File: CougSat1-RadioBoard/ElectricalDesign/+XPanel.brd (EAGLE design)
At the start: 79 x 90 mm, 66 parts, among them J1 ADCS Connector, J2 Low Gain +, J3 Low Gain -, J4 Low Gain Coax, J5 GPS Coax, J6 EPS Connector, U1 AD8515, U3 AD7291

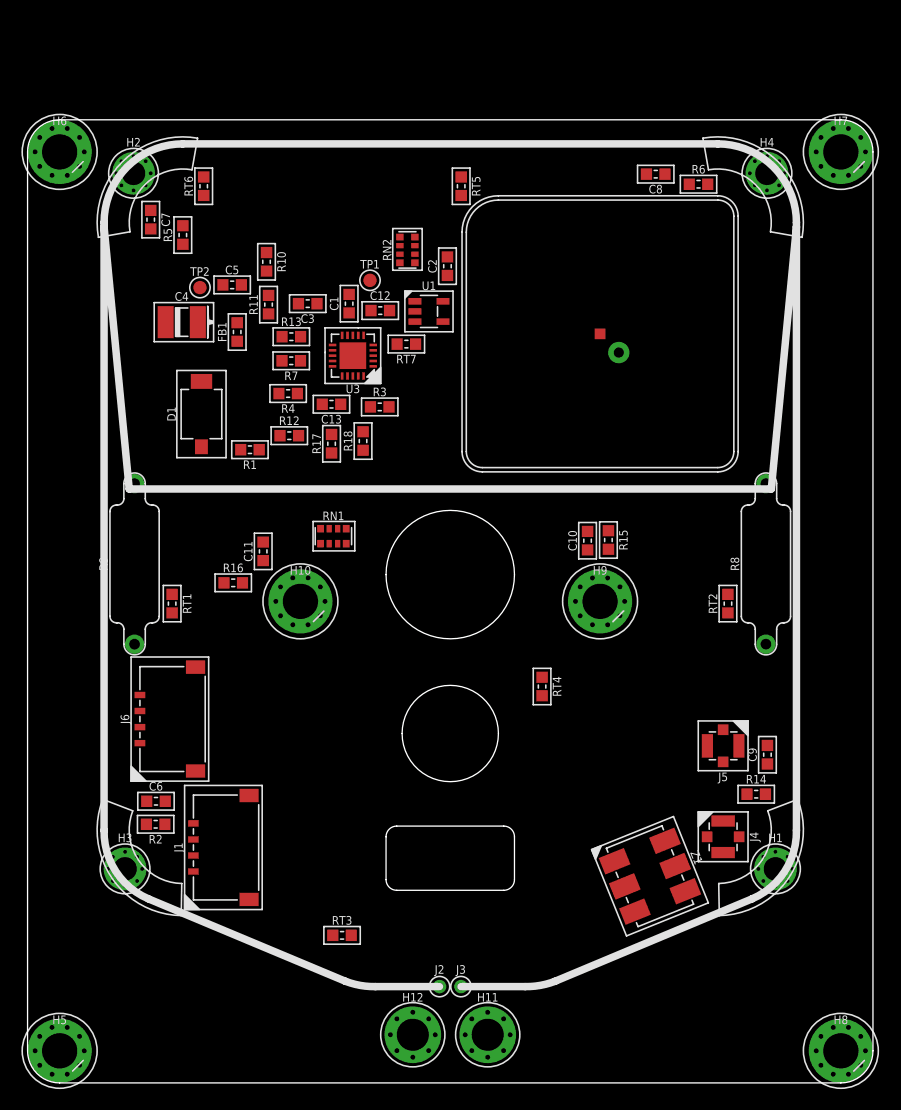
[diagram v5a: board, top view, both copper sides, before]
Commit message: Routed Initial Traces
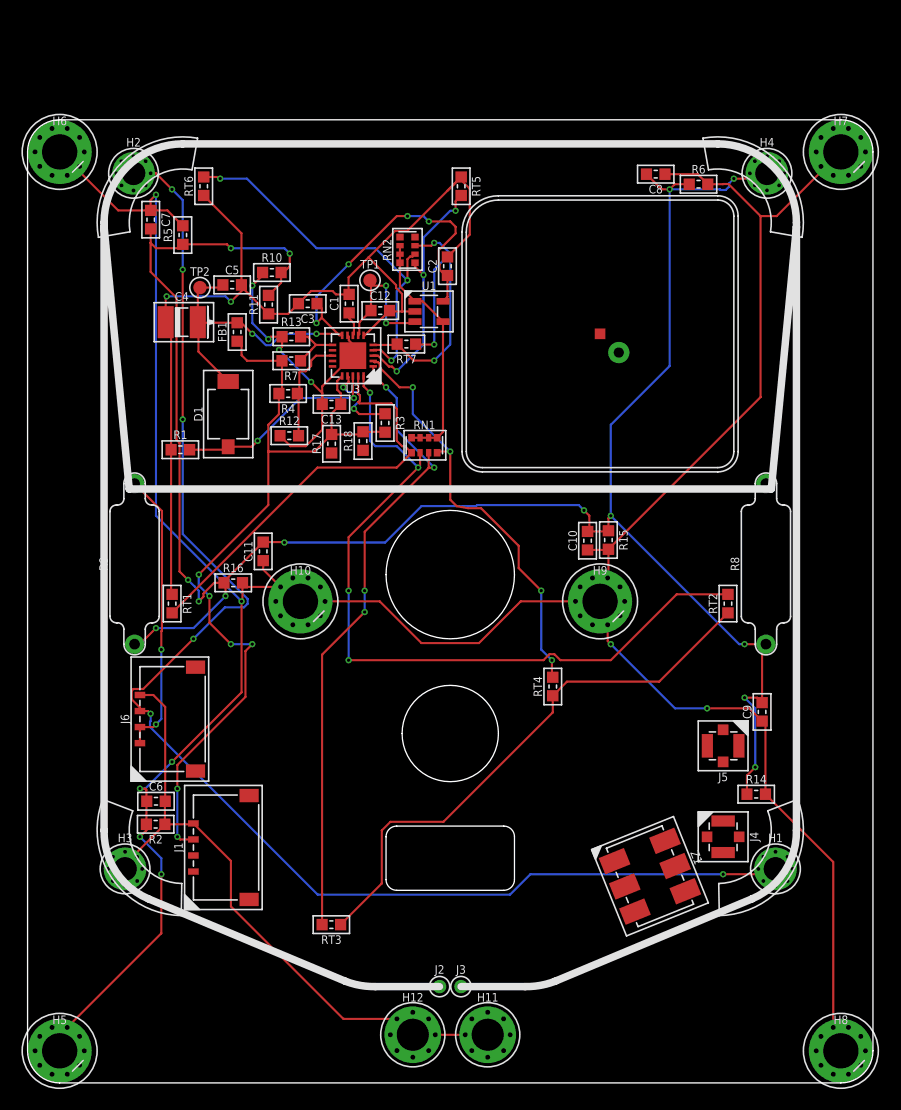
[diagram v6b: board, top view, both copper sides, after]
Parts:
- moved RN1 12.0 mm to (-2.42, 14.6)
- moved R1 6.50 mm to (-25.2, 14.2), turned to 0 degrees
- moved C9 4.03 mm to (29.1, -10.3)
- moved D1 2.50 mm to (-20.8, 17.5)
- moved R3 1.58 mm to (-6.09, 16.7), turned to 270 degrees
- moved RT3 1.41 mm to (-11.1, -30.2), turned to 180 degrees
- moved R10 1.12 mm to (-16.7, 30.7), turned to 0 degrees
- moved RT4 1.00 mm to (9.58, -7.96), turned to 90 degrees
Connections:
- net N$1 renamed DCAP
- net N$2 renamed PD_RST
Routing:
- net CHASSIS: track 0.00 -> 402.2 mm, vias 0 -> 8
- net PGND: track 0.00 -> 310.8 mm, vias 0 -> 14
- net AGND: track 0.00 -> 159.0 mm, vias 0 -> 3
- net SENSE: track 0.00 -> 156.2 mm, vias 0 -> 6
- net 3.3V: track 0.00 -> 79.0 mm, vias 0 -> 6
- net THERM-1: track 0.00 -> 72.5 mm, vias 0 -> 4
- net THERM-2: track 0.00 -> 60.6 mm, vias 0 -> 4
- net AVDD: track 0.00 -> 59.8 mm, vias 0 -> 6
- net THERM-3: track 0.00 -> 39.9 mm, vias 0 -> 4
- net THERM-0: track 0.00 -> 39.9 mm
- net THERM-5: track 0.00 -> 36.2 mm, vias 0 -> 3
- net DGND: track 0.00 -> 31.9 mm, vias 0 -> 4
- net VCC: track 0.00 -> 26.9 mm, vias 0 -> 2
- net THERM-4: track 0.00 -> 23.5 mm, vias 0 -> 3
- net AVREF: track 0.00 -> 22.7 mm
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
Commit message: Routed I2C
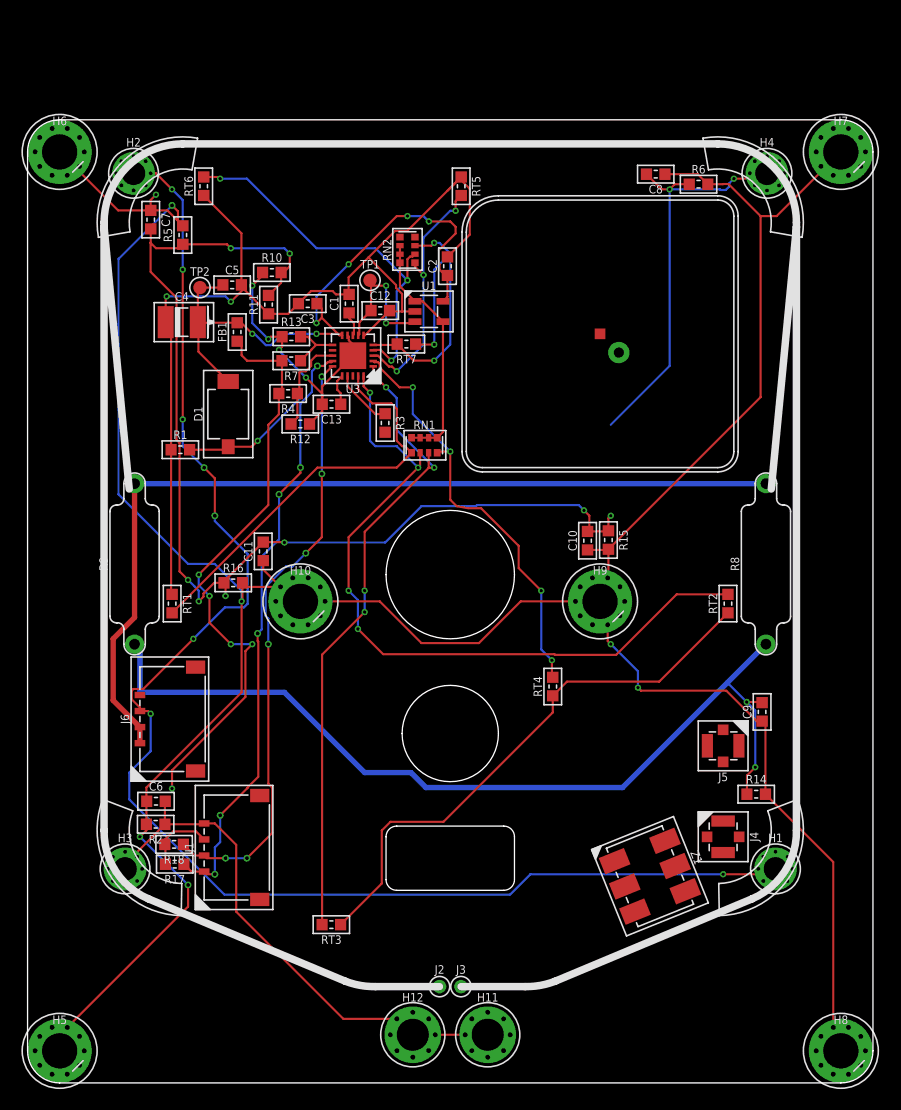
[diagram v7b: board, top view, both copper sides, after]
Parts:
- moved R17 41.9 mm to (-25.8, -24.6), turned to 180 degrees
- moved R18 41.6 mm to (-25.8, -22.7), turned to 180 degrees
- moved R12 1.50 mm to (-14.0, 16.6), turned to 180 degrees
- moved J1 1.00 mm to (-23.0, -23.0)
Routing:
- net VCC: track 26.9 -> 85.1 mm, vias 2 -> 0
- net I2C_SCL_ADCS: track 0.00 -> 56.6 mm, vias 0 -> 6
- net I2C_SDA_ADCS: track 0.00 -> 56.4 mm, vias 0 -> 6
- net PGND: track 310.8 -> 330.5 mm, vias 14 -> 12
- net 3.3V: track 79.0 -> 64.8 mm, vias 6 -> 5
- net CHASSIS: track 402.2 -> 409.7 mm, vias 8 -> 7
- net PHOTODIODE_SENSE: track 19.9 -> 12.8 mm, vias 2 -> 1
- net SENSE: track 156.2 -> 162.9 mm, vias 6 -> 8
- net DGND: track 31.9 -> 26.9 mm
- net THERM-1: track 72.5 -> 69.4 mm
- net PD_RST: track 7.78 -> 5.56 mm, vias 2 -> 0
- net THERM-0: track 39.9 -> 39.0 mm
- net ADC_AS1: track 10.2 -> 9.49 mm

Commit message: Updated RF Traces
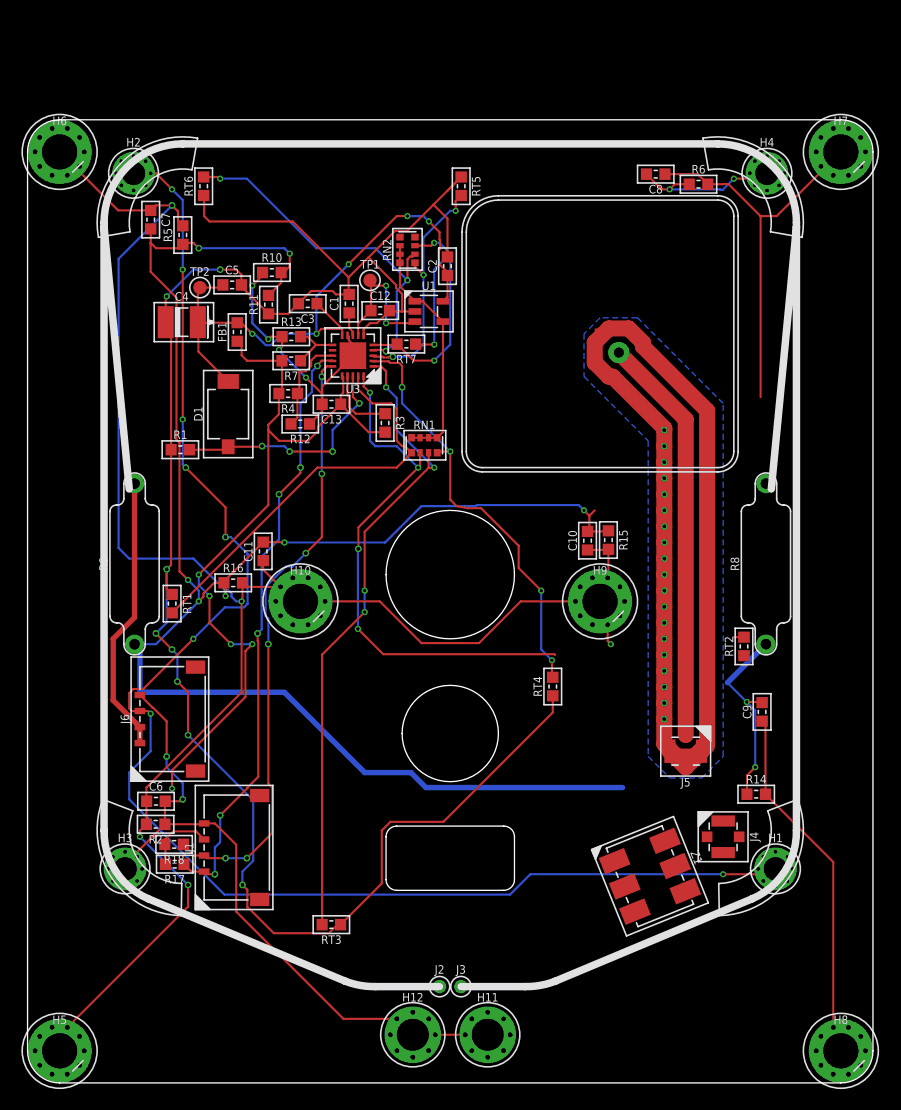
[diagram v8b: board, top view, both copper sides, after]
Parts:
- moved RT2 4.27 mm to (27.4, -4.21)
- moved J5 3.54 mm to (22.0, -14.0)
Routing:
- net RFGND-1: track 0.00 -> 94.7 mm, vias 0 -> 19
- net VCC: track 85.1 -> 26.1 mm
- net GPS_COAX: track 0.00 -> 38.3 mm
- net CHASSIS: track 409.7 -> 372.2 mm, vias 7 -> 5
- net AGND: track 159.0 -> 193.0 mm, vias 3 -> 9
- net THERM-1: track 69.4 -> 51.1 mm
- net PGND: track 330.5 -> 312.3 mm, vias 12 -> 13
- net 3.3V: track 64.8 -> 78.7 mm
- net PHOTODIODE_SENSE: track 12.8 -> 22.4 mm, vias 1 -> 4
- net AVDD: track 59.8 -> 57.5 mm, vias 6 -> 5
- net THERM-5: track 36.2 -> 34.6 mm
- net PD_RST: track 5.56 -> 6.74 mm
- net THERM-4: track 23.5 -> 22.4 mm
- net SENSE: track 162.9 -> 163.8 mm
- added copper zone on layer 16, net RFGND-1
